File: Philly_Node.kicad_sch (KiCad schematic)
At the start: 51 parts, among them J4 USB_C_Receptacle_USB2.0, J5 J-Link, Q4 Q_NMOS_GSD, T1 S2B-PH-SM4-TB, U1 MDBT50Q-U1MV2, U2 BQ25101, U7 E22-900M22S, Y1 32.768KHz

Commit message: Nearly done, final part number checks needed.
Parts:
- removed D6, D7, D8: LESD5D5_0CT1G, pager_parts:SOD-523_L1.2-W0.8-LS1.6-BI, symbol pager_parts:LESD5D5_0CT1G
- added C7: 100uf, Capacitor_SMD:CP_Elec_5x4.5, symbol Device:C_Polarized
- added F1: Polyfuse 3.5A, Fuse:Fuse_1206_3216Metric, symbol Device:Polyfuse_Small
- added J1: LED, Connector_PinSocket_1.00mm:PinSocket_1x03_P1.00mm_Vertical, symbol Connector_Generic:Conn_01x03
- added Q1: Q_Dual_NMOS_G1S2G2D2S1D1, Library:DFN-6-1EP_2x2mm_P0.65mm_EP_DUAL, symbol Philly:PJM05DN20DFA
- added R22, R24: 22, Resistor_SMD:R_0402_1005Metric, symbol Device:R_US
- added R23, R25: 1M, Resistor_SMD:R_0402_1005Metric, symbol Device:R_US
- D1, D2: value 1N5819WS -> B5819WT; footprint Diode_SMD:D_SOD-323 -> Diode_SMD:D_SOD-523; LCSC (none) -> C18216255
- J5: value J-Link -> Multi
- SOL1: renamed from T1; now fitted
- renumbered BT1 to BAT1
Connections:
- net GND: now also J5.7 (Pin_7), C7.2, Q1.1 (S), Q1.4 (S), R23.2, R25.2; no longer J5.5 (Pin_5), J5.9 (Pin_9)
- net P0.06_USER_BLUE: now also J1.1 (Pin_1)
- net P0.26_USER_RED: now also J1.3 (Pin_3)
- net P0.30_USER_GREEN: now also J1.2 (Pin_2)
- net VBAT_POL_PROT: now also J5.8 (Pin_8)
- net P1.11_TX: now reaches U1.4 (P1.11)
- net P1.11_TX: now also J5.6 (Pin_6)
- net P0.19: now reaches U1.42 (P0.19)
- net P0.19: now also R22.1
- net P0.20: now reaches U1.44 (P0.20)
- net P0.20: now also R24.1
- net P1.12_RX: now reaches U1.5 (P1.12)
- net P1.12_RX: now also J5.5 (Pin_5)
- net NMOS_2: now reaches J5.10 (Pin_10)
- net NMOS_2: now also Q1.3 (D), Q1.8 (D)
- net VBAT renamed VBAT_UNFUSED
- net VBAT_UNFUSED: now also C7.1, F1.1; no longer D3.2 (A)
- new net: Q1.2 (G), R22.2, R23.1
- new net: Q1.5 (G), R24.2, R25.1
- new net NMOS_1: J5.9 (Pin_9), Q1.6 (D), Q1.7 (D)
- new net VBAT_FUSED: D3.2 (A), F1.2
- no-connect marks 35 -> 28
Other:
- moved on the sheet: BAT1, D3, J5

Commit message: Added D0 button, NFC pads, and library files.
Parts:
- added C8: 0.1uF, Capacitor_SMD:C_0402_1005Metric, symbol Philly_Lib:C
- added NFC1, NFC2: TestPoint, Library:TestPoint_Pad_D0.75mm, symbol Philly_Lib:TestPoint
- added R8: 10k, Resistor_SMD:R_0402_1005Metric, symbol Philly_Lib:R_US
- added SW2: D0, Library:SW_Tactile_SPST_NO_Straight_TVAF44-N015C-R, symbol Philly_Lib:SW_Push
- BAT1: symbol Device:Battery_Cell -> Philly_Lib:Battery_Cell; LCSC (none) -> C295747
- C1, C2, C3: symbol Device:C -> Philly_Lib:C; LCSC (none) -> C19666
- C12, C13: symbol Device:C -> Philly_Lib:C
- C30, C9: symbol Seeed Studio XIAO nRF52840 v1.1-eagle-import:GroveX_C-0201 -> Philly_Lib:GroveX_C-0201; LCSC (none) -> C23630
- C4, C5: symbol Device:C -> Philly_Lib:C; LCSC (none) -> C1547
- C6: value 100nF -> 0.1uF; symbol Device:C -> Philly_Lib:C; LCSC (none) -> C1525
- C7: symbol Device:C_Polarized -> Philly_Lib:C_Polarized
- D1, D2, D3: symbol Device:D_Schottky -> Philly_Lib:D_Schottky
- D4, D5: symbol pager_parts:LESD5D5_0CT1G -> Philly_Lib:LESD5D5_0CT1G
- F1: symbol Device:Polyfuse_Small -> Philly_Lib:Polyfuse_Small
- H1, H2: symbol Mechanical:MountingHole -> Philly_Lib:MountingHole
- J1: symbol Connector_Generic:Conn_01x03 -> Philly_Lib:Conn_01x03; now not fitted
- J4: symbol Connector:USB_C_Receptacle_USB2.0 -> Philly_Lib:USB_C_Receptacle_USB2.0
- J5: footprint Connector_PinHeader_1.27mm:PinHeader_1x10_P1.27mm_Vertical -> Philly_Node_Lib:PinHeader_1x10_P1.27mm_Vertical; symbol Connector_Generic:Conn_02x05_Odd_Even -> Philly_Lib:Conn_02x05_Odd_Even; now not fitted
- L1: symbol Device:L -> Philly_Lib:L; LCSC (none) -> C1035
- LED1: symbol pager_parts:MHPA1010RGBDT -> Philly_Lib:MHPA1010RGBDT
- LED57: symbol pager_parts:KT-0603R -> Philly_Lib:KT-0603R
- Q1: symbol Philly:PJM05DN20DFA -> Philly_Lib:PJM05DN20DFA
- Q4: symbol Device:Q_NMOS_GSD -> Philly_Lib:Q_NMOS_GSD
- R1: symbol Device:R -> Philly_Lib:R; now not fitted
- R10, R11, R13, R16, R2, R20, R22, R24, R3, R39, R4, R9: symbol Device:R_US -> Philly_Lib:R_US
- R12, R18: symbol Seeed Studio XIAO nRF52840 v1.1-eagle-import:GroveX_R-0201 -> Philly_Lib:GroveX_R-0201
- R14: renamed from R8; value 1M_1% -> 1M; symbol Seeed Studio XIAO nRF52840 v1.1-eagle-import:GroveX_R-0201 -> Philly_Lib:GroveX_R-0201; LCSC (none) -> C26083
- R17: value 510k_1% -> 510k; symbol Seeed Studio XIAO nRF52840 v1.1-eagle-import:GroveX_R-0201 -> Philly_Lib:GroveX_R-0201; LCSC (none) -> C11616
- R23, R25: symbol Device:R_US -> Philly_Lib:R_US; LCSC (none) -> C26083
- R5: symbol Device:R -> Philly_Lib:R; LCSC C23186 -> C25905
- R6: symbol Device:R -> Philly_Lib:R; LCSC (none) -> C25905
- R7: symbol Seeed Studio XIAO nRF52840 v1.1-eagle-import:GroveX_R-0201 -> Philly_Lib:GroveX_R-0201; LCSC (none) -> C25744
- RESET1: symbol Switch:SW_Push -> Philly_Lib:SW_Push; LCSC C7471807 -> C22375376
- SOL1: symbol pager_parts:S2B-PH-K-S(LF)(SN) -> Philly_Lib:S2B-PH-K-S(LF)(SN); LCSC C173752 -> C295747
- U1: symbol RF_Module:MDBT50Q-1MV2 -> Philly_Lib:MDBT50Q-1MV2
- U2: symbol Seeed Studio XIAO nRF52840 v1.1-eagle-import:Seeed XIAO BLE_BQ25101_DSBGA_6_BQ25101_DSBGA_6 -> Philly_Lib:Seeed XIAO BLE_BQ25101_DSBGA_6_BQ25101_DSBGA_6
- U7: symbol pager_parts:E22-900M22S -> Philly_Lib:E22-900M22S
- Y1: symbol Device:Crystal -> Philly_Lib:Crystal
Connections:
- net GND: now also C8.2, SW2.2
- net VBAT_POL_PROT: now also R8.2
- net D0: now reaches U1.11 (P0.02/AIN0)
- net D0: now also C8.1, R8.1, SW2.1
- net NFC+: now reaches U1.52 (P0.09/NFC1)
- net NFC+: now also NFC1.1
- net NFC-: now reaches U1.54 (P0.10/NFC2)
- net NFC-: now also NFC2.1
- no-connect marks 28 -> 25

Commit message: Added courtyards, updated schematic to point to local lib footprints.
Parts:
- BAT1, SOL1: footprint Connector_JST:JST_PH_S2B-PH-SM4-TB_1x02-1MP_P2.00mm_Horizontal -> Philly_Lib:JST_PH_S2B-PH-SM4-TB_1x02-1MP_P2.00mm_Horizontal
- C1, C2, C3, C30, C9: footprint Capacitor_SMD:C_0603_1608Metric_Pad1.08x0.95mm_HandSolder -> Philly_Lib:C_0603_1608Metric
- C12, C13, C6, C8: footprint Capacitor_SMD:C_0402_1005Metric -> Philly_Lib:C_0402_1005Metric
- C4, C5: footprint Capacitor_SMD:C_0402_1005Metric_Pad0.74x0.62mm_HandSolder -> Philly_Lib:C_0402_1005Metric
- C7: footprint Capacitor_SMD:CP_Elec_5x4.5 -> Philly_Lib:CP_Elec_5x4.5
- D1, D2: footprint Diode_SMD:D_SOD-523 -> Philly_Lib:D_SOD-523
- D3: footprint Diode_SMD:D_SOD-323 -> Philly_Lib:D_SOD-323
- D4, D5: footprint pager_parts:SOD-523_L1.2-W0.8-LS1.6-BI -> Philly_Lib:SOD-523_L1.2-W0.8-LS1.6-BI
- F1: footprint Fuse:Fuse_1206_3216Metric -> Philly_Lib:Fuse_1206_3216Metric
- H1, H2: footprint MountingHole:MountingHole_2.5mm -> Philly_Lib:MountingHole_2.5mm
- J1: footprint Connector_PinSocket_1.00mm:PinSocket_1x03_P1.00mm_Vertical -> Philly_Lib:PinSocket_1x03_P1.00mm_Vertical
- J4: footprint Library:USB_C_Receptacle_GCT_USB4110_MODIFIED_FOR_PROTRSION -> Philly_Lib:USB_C_Receptacle_GCT_USB4110_MODIFIED_FOR_PROTRSION
- J5: footprint Philly_Node_Lib:PinHeader_1x10_P1.27mm_Vertical -> Philly_Lib:PinHeader_1x10_P1.27mm_Vertical
- L1: footprint Inductor_SMD:L_0603_1608Metric_Pad1.05x0.95mm_HandSolder -> Philly_Lib:L_0603_1608Metric
- LED1: footprint pager_parts:LED-ARRAY-SMD_4P-L1.0-W1.0-TR-RD -> Philly_Lib:LED-ARRAY-SMD_4P-L1.0-W1.0-TR-RD
- LED57: footprint pager_parts:LED0603-RD -> Philly_Lib:LED_0603_1608Metric
- NFC1, NFC2: footprint Library:TestPoint_Pad_D0.75mm -> Philly_Lib:TestPoint_Pad_D0.75mm
- Q1: footprint Library:DFN-6-1EP_2x2mm_P0.65mm_EP_DUAL -> Philly_Lib:DFN-6-1EP_2x2mm_P0.65mm_EP_DUAL
- Q4: footprint Package_TO_SOT_SMD:SOT-23-3 -> Philly_Lib:SOT-23-3
- R1: footprint Resistor_SMD:R_0603_1608Metric_Pad0.98x0.95mm_HandSolder -> Philly_Lib:R_0603_1608Metric
- R10, R11, R12, R13, R14, R16, R17, R18, R2, R20, R22, R23, R24, R25, R3, R39, R4, R5, R6, R7, R8, R9: footprint Resistor_SMD:R_0402_1005Metric -> Philly_Lib:R_0402_1005Metric
- RESET1: footprint Library:TS1187A26015 -> Philly_Lib:SW_Tactile_SPST_NO_Straight_TVAF44-N015C-R
- SW2: footprint Library:SW_Tactile_SPST_NO_Straight_TVAF44-N015C-R -> Philly_Lib:SW_Tactile_SPST_NO_Straight_TVAF44-N015C-R
- U1: footprint RF_Module:Raytac_MDBT50Q -> Philly_Lib:Raytac_MDBT50Q
- U2: footprint Philly_Node_Lib:YFP0006AFAV -> Philly_Lib:YFP0006AFAV
- U7: footprint pager_parts:WIRELM-SMD_E22-900M22S -> Philly_Lib:WIRELM-SMD_E22-900M22S
- Y1: footprint Crystal:Crystal_SMD_MicroCrystal_CC7V-T1A-2Pin_3.2x1.5mm -> Philly_Lib:Crystal_SMD_MicroCrystal_CC7V-T1A-2Pin_3.2x1.5mm

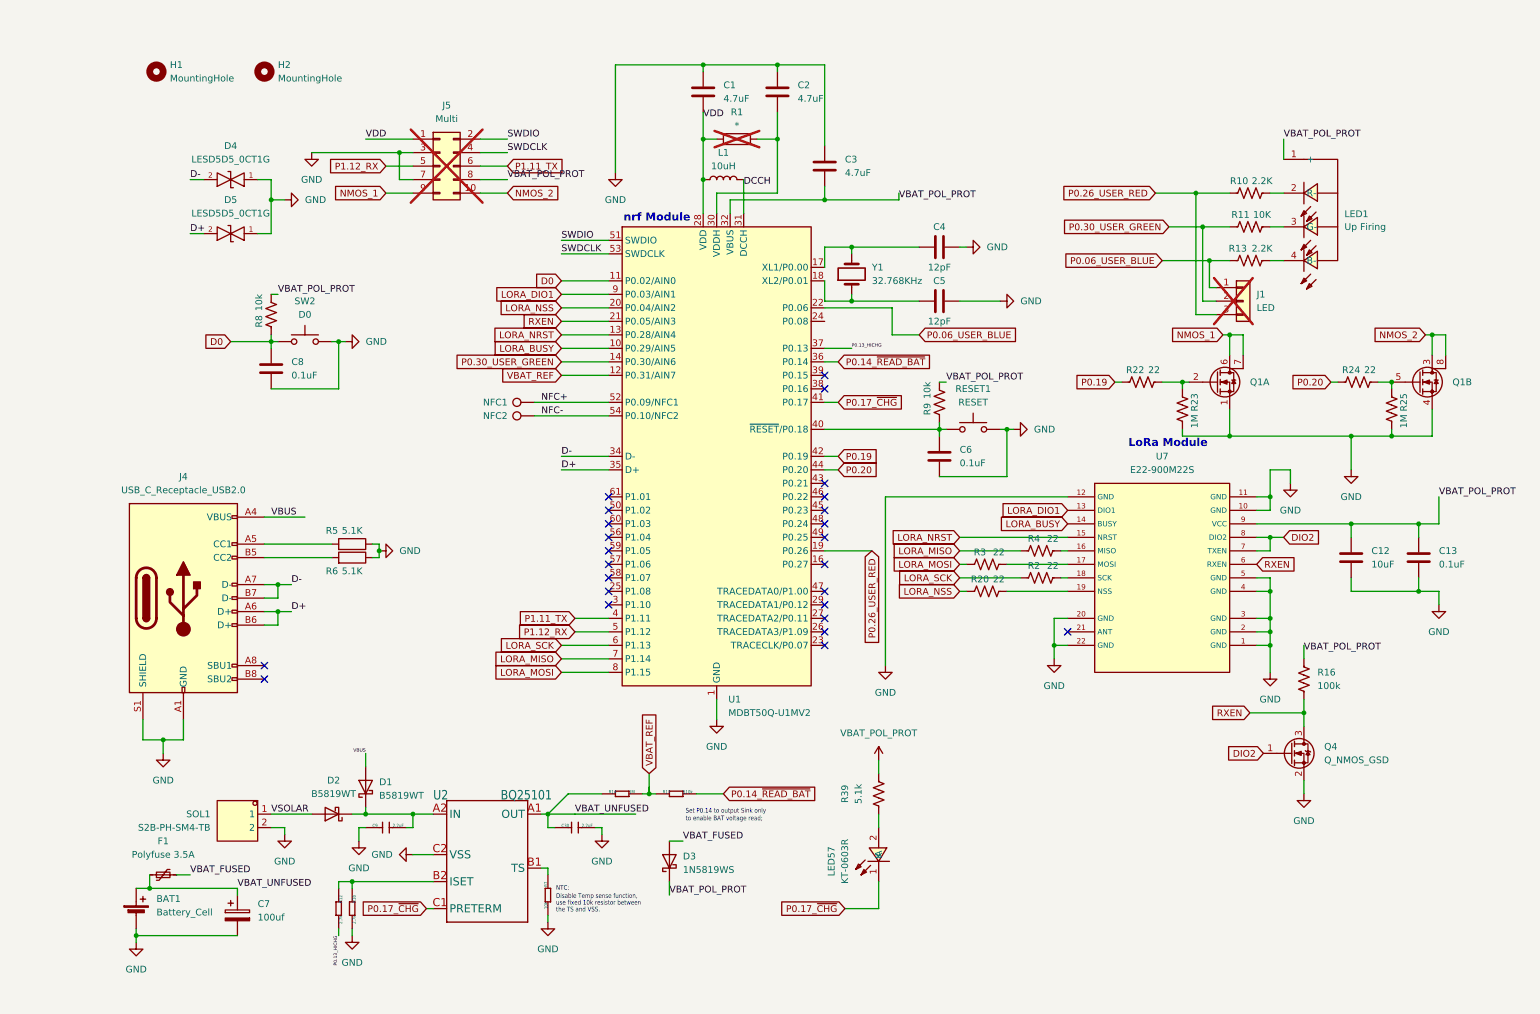
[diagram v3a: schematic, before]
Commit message: changed to BQ25176JDSGR charge IC
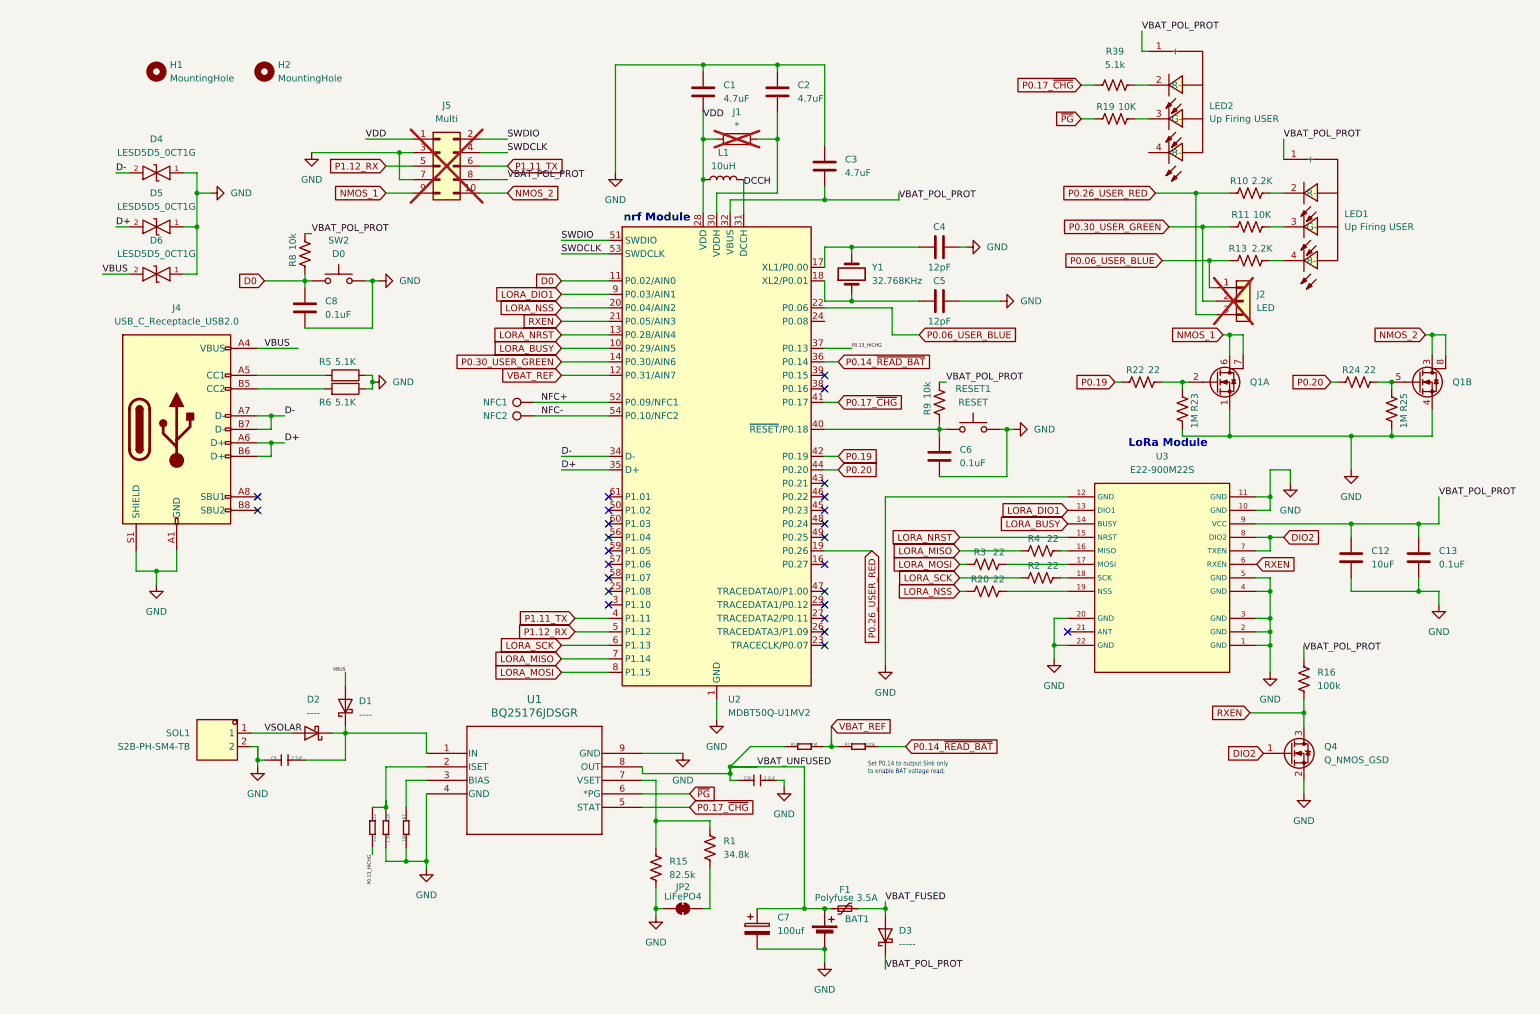
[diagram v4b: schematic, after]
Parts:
- removed LED57: KT-0603R, Philly_Lib:LED_0603_1608Metric, symbol Philly_Lib:KT-0603R
- removed U2: BQ25101, Philly_Lib:YFP0006AFAV, symbol Philly_Lib:Seeed XIAO BLE_BQ25101_DSBGA_6_BQ25101_DSBGA_6
- added D6: LESD5D5_0CT1G, Philly_Lib:SOD-523_L1.2-W0.8-LS1.6-BI, symbol Philly_Lib:LESD5D5_0CT1G
- added JP2: LiFePO4, Philly_Lib:SolderJumper, symbol Jumper:SolderJumper_2_Bridged
- added LED2: MHPA1010RGBDT, Philly_Lib:LED-ARRAY-SMD_4P-L1.0-W1.0-TR-RD, symbol Philly_Lib:MHPA1010RGBDT
- added R1: 34.8k, Philly_Lib:R_0402_1005Metric, symbol Philly_Lib:R_US
- added R15: 82.5k, Philly_Lib:R_0402_1005Metric, symbol Philly_Lib:R_US
- added R19: 10K, Philly_Lib:R_0402_1005Metric, symbol Philly_Lib:R_US
- added U1: BQ25176JDSGR, WSON_MDSGR_TEX, symbol 2026-02-13_14-29-23:BQ25176JDSGR
- BAT1: value Battery_Cell -> S2B-PH-SM4-TB
- C30, C9: footprint Philly_Lib:C_0603_1608Metric -> Philly_Lib:C_0402_1005Metric; LCSC C23630 -> C72203
- D1, D2: value B5819WT -> ----; LCSC C18216255 -> (none)
- D3: value 1N5819WS -> -----
- J1: renamed from R1; footprint Philly_Lib:R_0603_1608Metric -> Philly_Lib:R_0402_1005Metric
- LED1: Note Up Firing -> Up Firing USER
- R12: value 2.7k -> 510; LCSC C25885 -> C25123
- R18: value 2.7k -> 1.5k; LCSC C25885 -> C25867
- renumbered J1 to J2, U1 to U2, U7 to U3
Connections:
- net GND: now also D6.1, JP2.1 (A), R15.2, U1.4 (GND), U1.9 (GND)
- net P0.17_~{CHG}: now also R39.1, U1.5 (STAT)
- net VBAT_POL_PROT: now also LED2.1 (+); no longer R39.1
- net VBAT_UNFUSED: now also U1.8 (OUT)
- net VBUS: now also D6.2
- net at R12.1, R18.1: now also U1.2 (ISET)
- net at C9.2, D1.1 (K), D2.1 (K): now also U1.1 (IN)
- net at R39.2: now also LED2.2 (R-)
- net at R7.1: now also U1.3 (BIAS)
- new net: R1.1, R15.1, U1.7 (VSET)
- new net: JP2.2 (B), R1.2
- new net: LED2.3 (G-), R19.2
- new net ~{PG}: R19.1, U1.6 (*PG)
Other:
- note removed: "Disable Temp sense function,"
- note removed: "NTC:"
- note removed: "the TS and VSS."
- note removed: "use fixed 10k resistor between"
- moved on the sheet: BAT1, C30, C7, C8, C9, D1, D2, D4, D5, F1, J4, R12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

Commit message: Changes to powerpath, added test points for battery/solar, misc other.
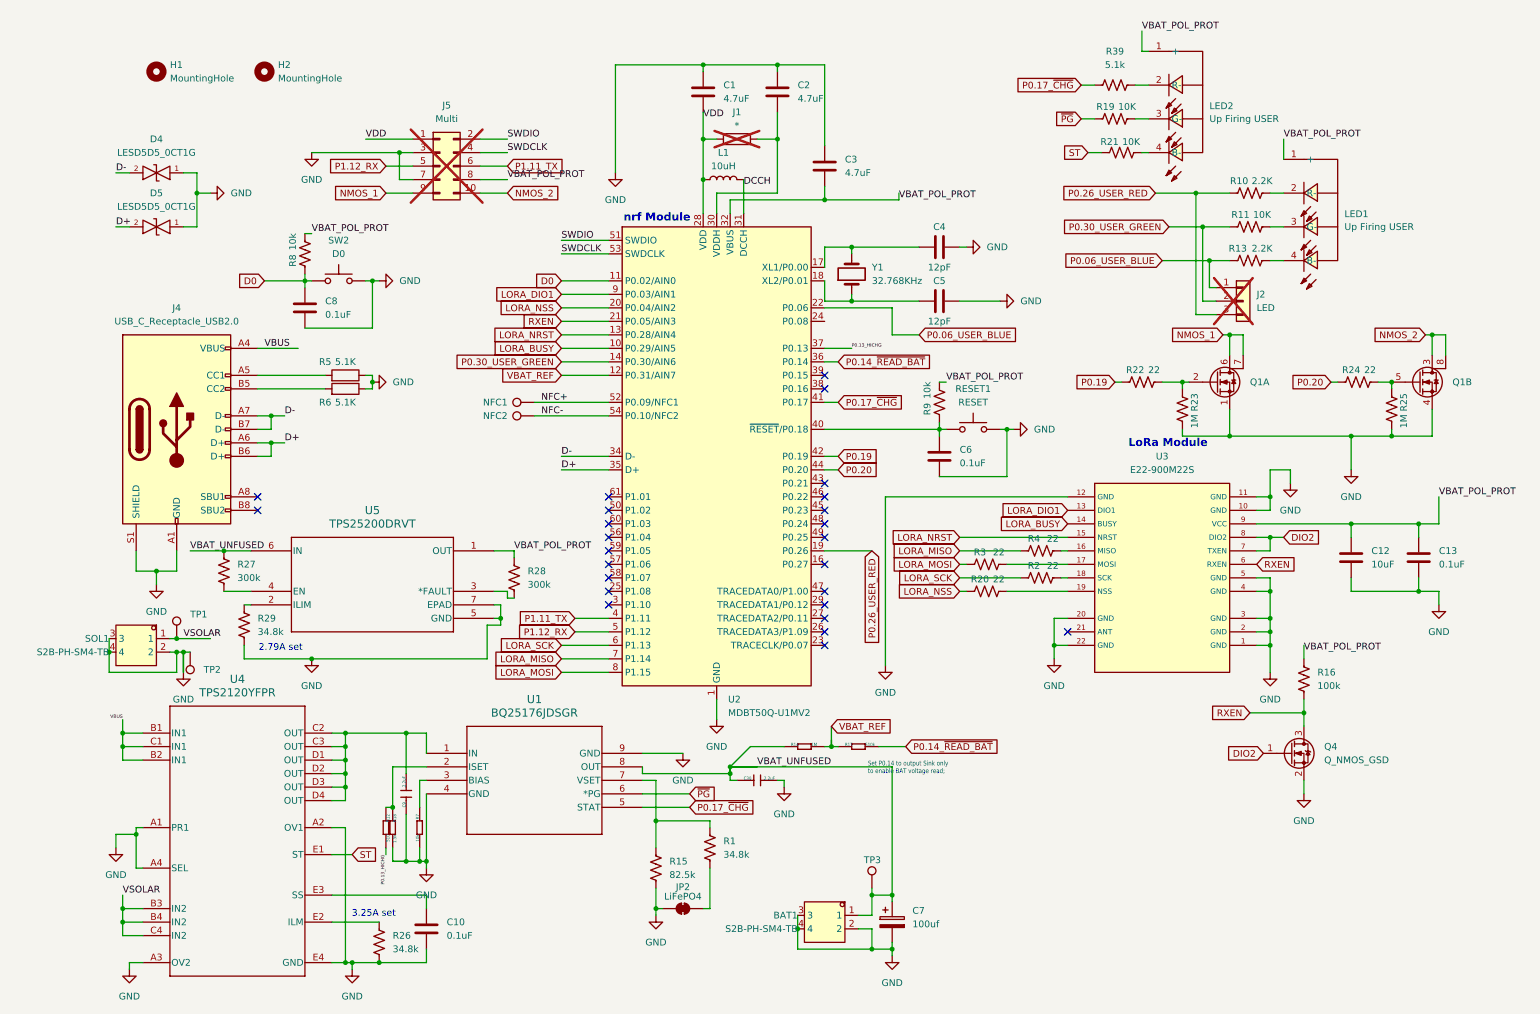
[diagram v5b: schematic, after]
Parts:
- removed BAT1: S2B-PH-SM4-TB, Philly_Lib:JST_PH_S2B-PH-SM4-TB_1x02-1MP_P2.00mm_Horizontal, symbol Philly_Lib:Battery_Cell
- removed D1, D2: ----, Philly_Lib:D_SOD-523, symbol Philly_Lib:D_Schottky
- removed D3: -----, Philly_Lib:D_SOD-323, symbol Philly_Lib:D_Schottky
- removed D6: LESD5D5_0CT1G, Philly_Lib:SOD-523_L1.2-W0.8-LS1.6-BI, symbol Philly_Lib:LESD5D5_0CT1G
- removed F1: Polyfuse 3.5A, Philly_Lib:Fuse_1206_3216Metric, symbol Philly_Lib:Polyfuse_Small
- removed SOL1: S2B-PH-SM4-TB, Philly_Lib:JST_PH_S2B-PH-SM4-TB_1x02-1MP_P2.00mm_Horizontal, symbol Philly_Lib:S2B-PH-K-S(LF)(SN)
- added BAT1, SOL1: S2B-PH-SM4-TB, pager_parts:CONN-TH_S2B-PH-K-S-LF-SN, symbol Philly_Lib:S2B-PH-K-S(LF)(SN)_1
- added C10: 0.1uF, Philly_Lib:C_0402_1005Metric, symbol Philly_Lib:C
- added R21: 10K, Philly_Lib:R_0402_1005Metric, symbol Philly_Lib:R_US
- added R26, R29: 34.8k, Philly_Lib:R_0402_1005Metric, symbol Philly_Lib:R_US
- added R27, R28: 300k, Philly_Lib:R_0402_1005Metric, symbol Philly_Lib:R_US
- added TP1, TP2, TP3: TestPoint, Philly_Lib:TestPoint_Pad_1.0x1.0mm, symbol Philly_Lib:TestPoint
- added U4: TPS2120YFPR, Philly_Lib:YFP0020AAAA, symbol Philly_Lib:TPS2120YFPR
- added U5: TPS25200DRVT, Philly_Node_Lib:DRV6_1X1P6_TEX, symbol Philly_Lib:TPS25200DRVT
- JP2: symbol Jumper:SolderJumper_2_Bridged -> Philly_Lib:SolderJumper_2_Bridged
- RESET1: LCSC C22375376 -> C19270949
- U1: symbol 2026-02-13_14-29-23:BQ25176JDSGR -> Philly_Lib:BQ25176JDSGR
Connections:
- net GND: now also BAT1.2, BAT1.3, BAT1.4, C10.2, R26.2, R29.2, SOL1.2, SOL1.3, SOL1.4, TP2.1, U4.A1 (PR1), U4.A2 (OV1), U4.A3 (OV2), U4.A4 (SEL), U4.E4 (GND), U5.5 (GND), U5.7 (EPAD)
- net VBAT_POL_PROT: now also R28.1, U5.1 (OUT)
- net VBAT_UNFUSED: now also BAT1.1, R27.1, TP3.1, U5.6 (IN)
- net VBUS: now also U4.B1 (IN1), U4.B2 (IN1), U4.C1 (IN1)
- net VSOLAR: now also SOL1.1, TP1.1, U4.B3 (IN2), U4.B4 (IN2), U4.C4 (IN2)
- net at C9.2, U1.1 (IN): now also U4.C2 (OUT), U4.C3 (OUT), U4.D1 (OUT), U4.D2 (OUT), U4.D3 (OUT), U4.D4 (OUT)
- net at LED2.4 (B-): now also R21.2
- new net: R26.1, U4.E2 (ILM)
- new net: C10.1, U4.E3 (SS)
- new net: R29.1, U5.2 (ILIM)
- new net: R28.2, U5.3 (*FAULT)
- new net: R27.2, U5.4 (EN)
- new net ST: R21.1, U4.E1 (ST)
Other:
- note added: "2.79A set"
- note added: "3.25A set"
- moved on the sheet: C7, C9, R12, R18, R7

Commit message: Production order. Changed to Amphenol USB-C connector from clone.
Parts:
- BAT1: LCSC C47647 -> C968533
- J4: LCSC C5143397 -> C34260841
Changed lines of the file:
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@@
 			)
 		)
-		(property "LCSC" "C47647"
+		(property "LCSC" "C968533"
 			(at 144.78 182.88 0)
 			(effects
@@
 			)
 		)
-		(property "LCSC" "C5143397"
+		(property "LCSC" "C34260841"
 			(at 27.94 91.44 0)
 			(effects
